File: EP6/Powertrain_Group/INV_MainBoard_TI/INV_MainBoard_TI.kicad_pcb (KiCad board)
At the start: 4 copper layers, 100 x 92 mm, 297 parts, among them IC1 LM26420Q0XMHX_NOPB, J1 FX26-30P-1SV, J10 CAN, J11 CAN, J12 CAN, J13 motorTemp, J14 LVBattery, J15 PWMDAC, J2 motorSense, J3 LVBattery, J4 JTAG, J5 current_DC, J6 to PhaseIsense, J7 phase control monitor, J8 current, J9 CAN, Q1 2N7002, Q2 2N7002, SW1 TS-1187A-B-A-B, SW2 BUT39, SW3 BUT58, U10 LM2903, U11 LM2903, U12 LM2903, U13 LM2903, U14 INA333AIDGK, U15 LM2903, U16 LM324D, U18 OPA340NA, U2 TPS5430DDAR, U22 tms320f28377s, U23 REF3133AQDBZRQ1, U24 REF3133AQDBZRQ1, U3 INA333AIDGK, U4 TCAN1042VDRQ1, U5 CAT24C256, U6 TCAN1042VDRQ1, U7 INA333AIDGK, U8 INA333AIDGK, U9 INA333AIDGK, Y1 ABM3BAIG-10.000MHZ-12-1Z-T

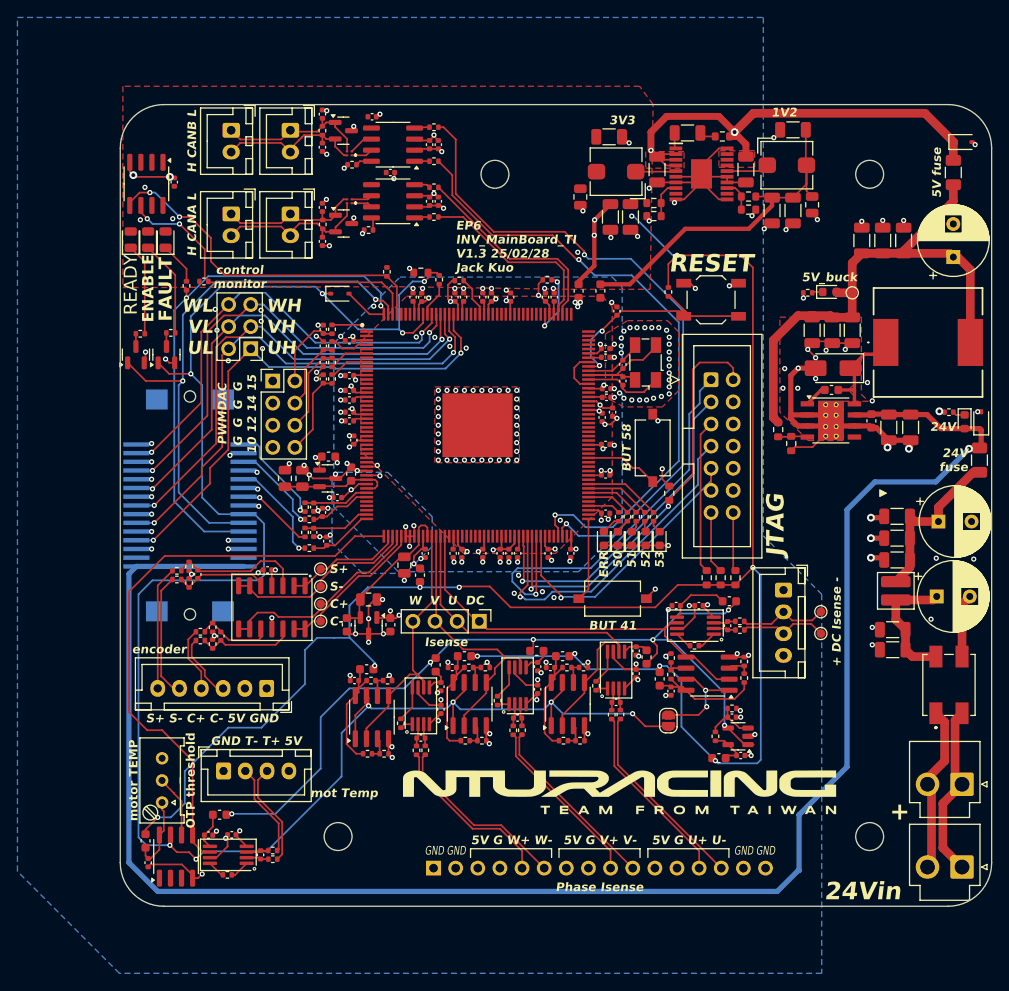
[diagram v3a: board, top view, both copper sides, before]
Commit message: update INV_MainBoard_TI to V1.4
update for JLCPCB parts
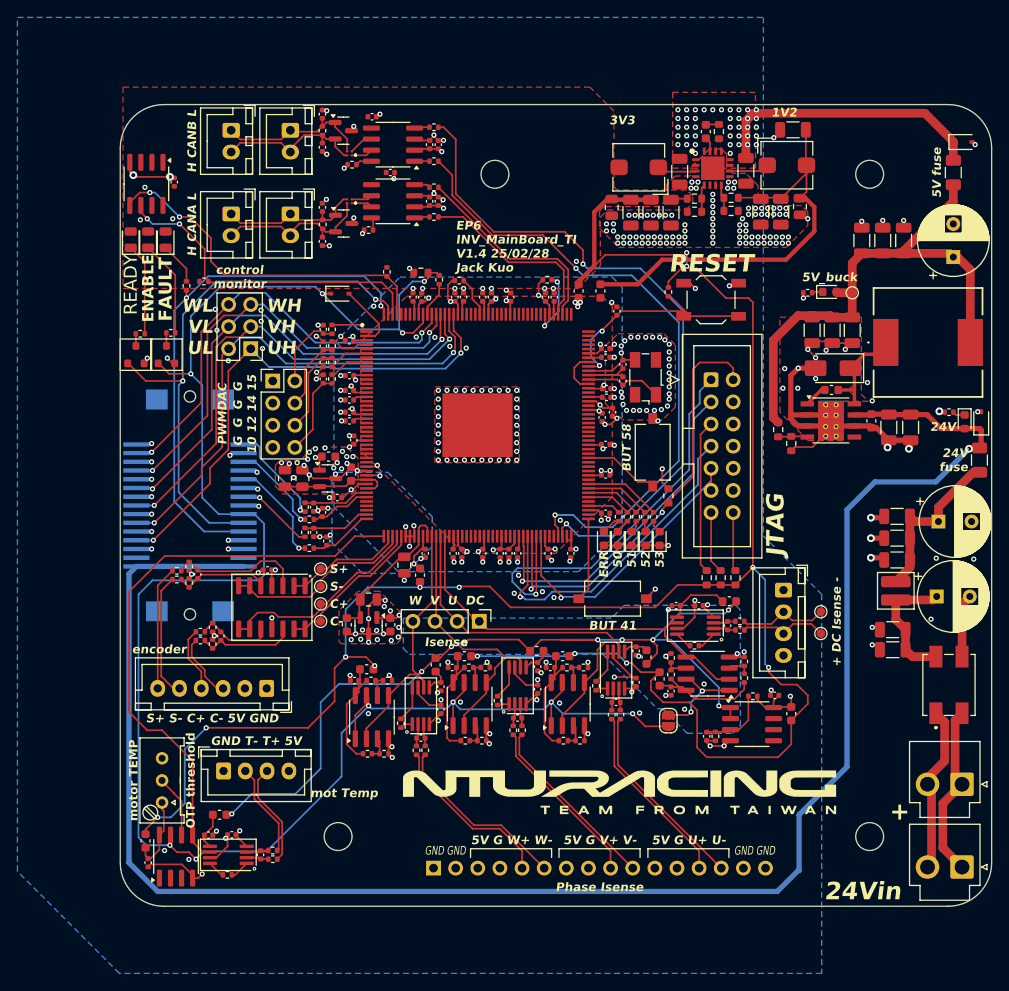
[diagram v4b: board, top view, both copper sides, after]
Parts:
- C38: footprint Capacitor_SMD:C_1206_3216Metric -> Capacitor_SMD:C_0603_1608Metric
- D11: value LED50 -> RED LED 50
- D12: value LED50 -> YELLOW LED 51
- D13: value LED50 -> GREEN LED 52
- D14: value LED50 -> WHITE LED 53
- D3: value 27V BZT52C27 -> 27V C22375300
- D5: value 5.6V BZT52C5V6S -> 5.6V_C19077441
- D9: value RED -> RED LED
- FB12, FB14: value FerriteBead -> GZ1608D601TF
- IC1: value LM26420Q0XMHX_NOPB -> LM26420; footprint SamacSys_Parts_EP6:SOP65P640X120-21N -> SamacSys_Parts_EP6:QFN65P400X400X80-17N
- Q1, Q2: footprint Package_TO_SOT_SMD:SOT-23 -> PCM_Package_TO_SOT_SMD_AKL:SOT-23
- R15, R16, R70, R71: value 20R -> 22R
- R33, R51, R56, R58: value 28k -> 27k
- R8: value 47k 1% -> 47k
- R9: value 15k 1% -> 15k
- U10, U11, U12, U13, U15: value LM2903 -> LM393
- U18: value OPA340NA -> NE5532; footprint Package_TO_SOT_SMD:SOT-23-5 -> Package_SO:SOIC-8_3.9x4.9mm_P1.27mm
- U23, U24: value REF3133AQDBZRQ1 -> REF3133AIDBZR
- U5: value CAT24C256 -> CAT24C512
- Y1: value ABM3BAIG-10.000MHZ-12-1Z-T -> 10MHz SMD5032-4P
- moved FB4 9.74 mm to (185.5, 126.9), turned to 90 degrees
- moved C95 9.05 mm to (167.1, 69.4), turned to -90 degrees
- moved C103 7.93 mm to (183.6, 124.8), turned to 180 degrees
- moved R25 6.30 mm to (181.1, 124.9), turned to 180 degrees
- moved C55 4.68 mm to (169.4, 69.4)
- moved R14 4.68 mm to (174.4, 69.3)
- moved R2 4.68 mm to (174.4, 67.8)
- moved C39 4.68 mm to (171.7, 69.4)
- moved C110 3.79 mm to (164.9, 68.8)
- moved R26 3.72 mm to (176.8, 129.5), turned to -90 degrees
- moved C104 3.64 mm to (175.8, 129.5), turned to -90 degrees
- moved L2 2.65 mm to (168.0, 64.2)
- moved C1 2.61 mm to (172.7, 64.7)
- moved U18 2.13 mm to (181.0, 128.1), turned to 0 degrees
- moved C38 2.11 mm to (175.7, 60.1), turned to -90 degrees
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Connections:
- C103 pad 1: Net-(U18-V+) -> Net-(U18C-V+)
- D15 pad 2: /FLTN -> /OCPFLTN
- FB4 pad 2: Net-(U18-V+) -> Net-(U18C-V+)
- IC1 pad 1: Net-(IC1-VINC) -> +5V
- IC1 pad 10: GND -> Net-(IC1-SW2)
- IC1 pad 11: GND -> +5V
- IC1 pad 12: /Power/1V2_powerGood -> +5V
- IC1 pad 13: Net-(IC1-FB2) -> +5V
- IC1 pad 15: GND -> Net-(IC1-VINC)
- IC1 pad 16: Net-(IC1-SW2) -> +5V
- IC1 pad 17: +5V -> GND
- IC1 pad 3: +5V -> Net-(IC1-SW1)
- IC1 pad 4: +5V -> GND
- IC1 pad 5: Net-(IC1-SW1) -> Net-(IC1-FB1)
- IC1 pad 6: GND -> /Power/3V3_powerGood
- IC1 pad 7: GND -> /Power/1V2_powerGood
- IC1 pad 8: Net-(IC1-FB1) -> Net-(IC1-FB2)
- IC1 pad 9: /Power/3V3_powerGood -> GND
- R25 pad 1: Net-(U18-V+) -> Net-(U18C-V+)
- U18 pad 2: GND -> /Isense&motT_OCP&OTP/Vref_1.65V
- U18 pad 4: /Isense&motT_OCP&OTP/Vref_1.65V -> GND
- U18 pad 5: Net-(U18-V+) -> unconnected-(U18B-+-Pad5)
- U22 pad 2: unconnected-(U22C-GPIO11-Pad2) -> /OCPFLTN
- Y1 pad 2: Net-(U22B-VSSOSC) -> GND
- Y1 pad 4: Net-(U22B-VSSOSC) -> GND
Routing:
- net GND: track 271.7 -> 237.0 mm, vias 252 -> 364
- net +5V: track 92.5 -> 72.7 mm, vias 13 -> 53
- net +3V3: track 229.4 -> 248.4 mm
- net +1V2: track 41.0 -> 50.3 mm
- net Net-(U18C-V+): track 0.00 -> 7.60 mm, vias 0 -> 1
- net /OCPFLTN: track 0.00 -> 7.45 mm
- net Net-(U22B-VSSOSC): track 14.9 -> 8.27 mm
- net /FLTN: track 65.9 -> 60.9 mm
- net Net-(U18-V+): track 4.66 -> 0.00 mm
- net Net-(U18A-+): track 6.29 -> 8.10 mm
- net Net-(IC1-FB1): track 4.47 -> 3.17 mm
- net /Isense&motT_OCP&OTP/OCPnode/GateEnable: track 12.2 -> 11.2 mm
- net Net-(U22B-X1): track 6.76 -> 5.86 mm
- net /MCU/CANB_RX: track 77.4 -> 78.1 mm
- net /Isense&motT_OCP&OTP/Vref_1.65V: track 95.8 -> 96.5 mm, vias 6 -> 9
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- added copper zone on B.Cu, net /Isense&motT_OCP&OTP/Vref_1.65V
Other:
- board text added: "EP6 INV_MainBoard_TI V1.4 25/02/28 Jack Kuo"
- board text removed: "EP6 INV_MainBoard_TI V1.3 25/02/28 Jack Kuo"
